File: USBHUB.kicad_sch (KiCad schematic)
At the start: 0 parts

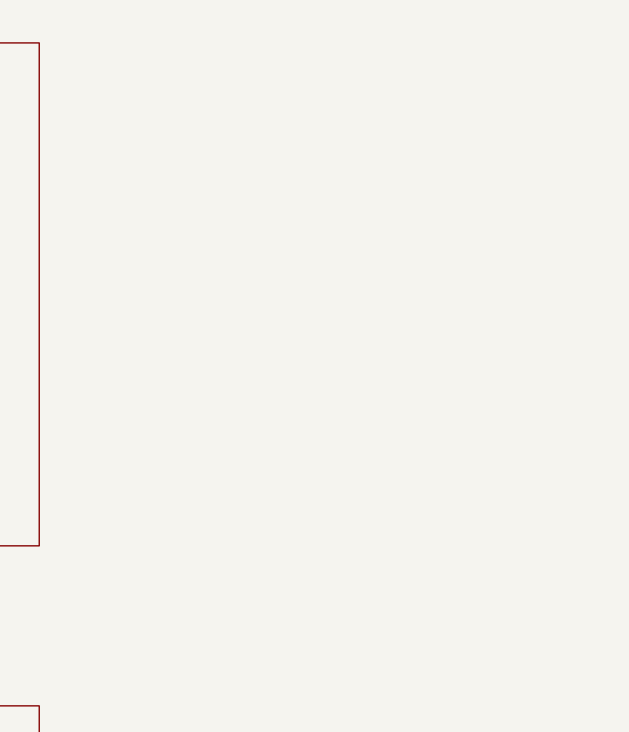
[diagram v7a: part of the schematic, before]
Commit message: add RTL8153
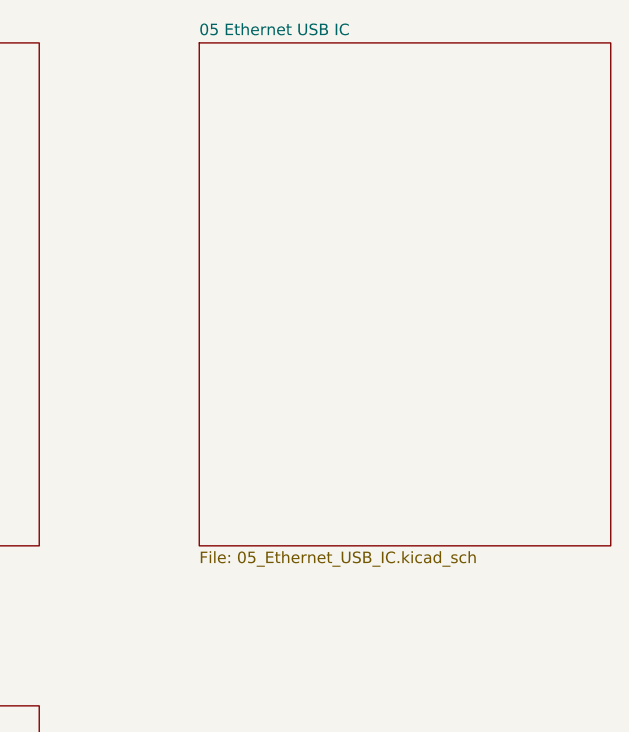
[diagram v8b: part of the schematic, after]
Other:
- added sheet 05 Ethernet USB IC (05_Ethernet_USB_IC.kicad_sch)
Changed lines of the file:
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@@
+    )
+  )
+  (sheet (at 146.05 22.86) (size 45.72 55.88) (fields_autoplaced)
+    (stroke (width 0.1524) (type solid))
+    (fill (color 0 0 0 0.0000))
+    (property "Sheetname" "05 Ethernet USB IC" (at 146.05 22.1484 0)
+      (effects (font (size 1.27 1.27)) (justify left bottom))
+    )
+    (property "Sheetfile" "05_Ethernet_USB_IC.kicad_sch" (at 146.05 79.3246 0)
+      (effects (font (size 1.27 1.27)) (justify left top))
+    )
+    (instances
+      (project "USBHUB"
+        (path "/d5edc647-9ac3-4ac1-ab8a-57c77be3f4d3" (page "8"))
+      )
     )
   )
